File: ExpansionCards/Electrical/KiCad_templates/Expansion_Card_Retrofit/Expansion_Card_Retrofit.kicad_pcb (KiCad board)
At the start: 2 copper layers, 24 x 27.3 mm, 30 parts, among them J1 HDMI_A, P2 USB_C_Plug, U1 MS2130, U2 GD25D05CT, U3 USBLC6-2P6, Y1 Crystal

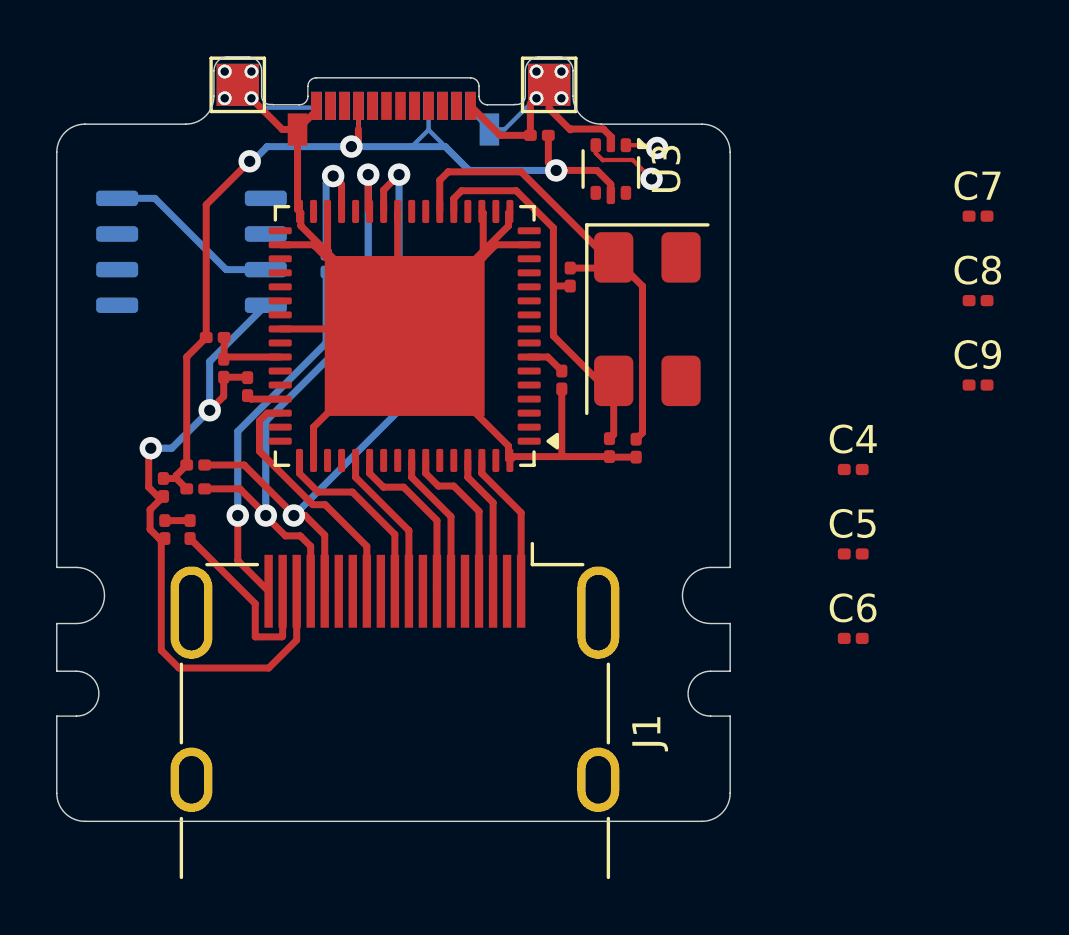
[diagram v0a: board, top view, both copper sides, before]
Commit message: Change PCB to 4 Layer and improve routing
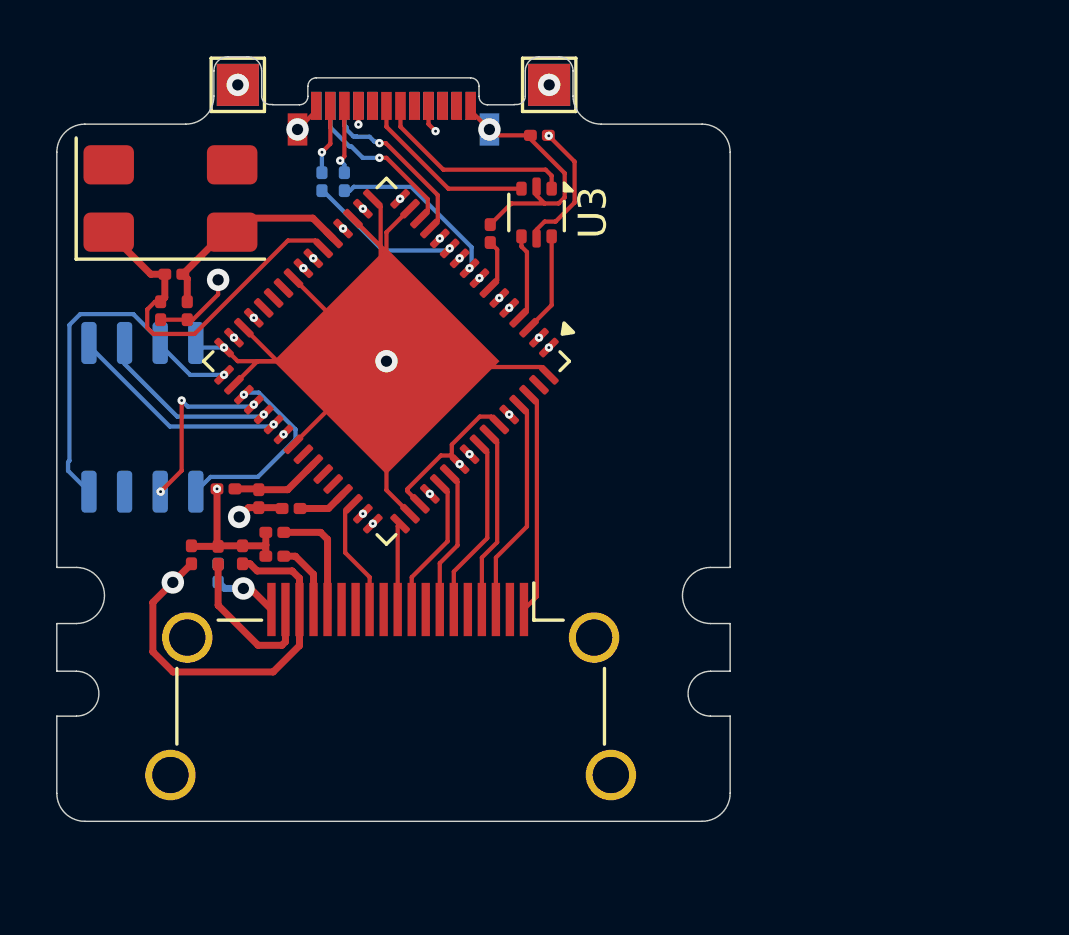
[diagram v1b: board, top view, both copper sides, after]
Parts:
- removed C4, C5, C6, C7: C_Small, Capacitor_SMD:C_0201_0603Metric
- C8, C9: moved to B.Cu
- J1: footprint Connector_Video:HDMI_A_Molex_208658-1001_Horizontal -> Connector_Video:HDMI_A_Amphenol_10029449-x01xLF_Horizontal
- moved C9 24.5 mm to (137.4, 131.8), turned to -90 degrees
- moved C8 23.0 mm to (138.2, 131.8), turned to -90 degrees
- moved C11 17.6 mm to (131.7, 136.3)
- moved Y1 17.5 mm to (132.1, 132.3), turned to 0 degrees
- moved C10 15.8 mm to (132.7, 136.3)
- moved R9 14.1 mm to (132.2, 135.1), turned to 180 degrees
- moved R3 11.7 mm to (133.8, 145.7)
- moved U2 6.15 mm to (131.1, 140.2), turned to -90 degrees
- moved R1 5.81 mm to (143.4, 133.6), turned to 90 degrees
- moved R7 5.41 mm to (134.0, 142.7)
- moved R8 4.82 mm to (135.2, 143.1)
- moved R2 4.61 mm to (136.3, 143.4), turned to 180 degrees
- moved R5 3.70 mm to (135.8, 144.2)
- moved R6 3.70 mm to (135.8, 145.1)
- moved C3 3.70 mm to (134.6, 145.1)
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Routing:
- net Net-(U2-VCC): track 6.35 -> 31.9 mm, vias 0 -> 4
- net GND: track 109.2 -> 85.4 mm, vias 10 -> 9
- net Net-(J1-SDA): track 21.3 -> 2.58 mm, vias 2 -> 0
- net Net-(J1-SCL): track 22.6 -> 4.16 mm, vias 2 -> 0
- net Net-(U1-AVDD11-Pad24): track 0.00 -> 15.5 mm, vias 0 -> 2
- net Net-(U1-AVDD25-Pad20): track 0.00 -> 12.4 mm, vias 0 -> 3
- net Net-(J1-HPD): track 13.1 -> 2.31 mm
- net Net-(U1-DVDD11-Pad18): track 0.00 -> 10.2 mm, vias 0 -> 2
- net SPICS: track 0.00 -> 7.90 mm, vias 0 -> 1
- net SPIMOSI: track 0.00 -> 7.10 mm, vias 0 -> 1
- net Net-(U1-AVDD33-Pad48): track 0.00 -> 6.89 mm, vias 0 -> 4
- net Net-(U1-XTIN): track 14.1 -> 7.53 mm
- net SPIMISO: track 0.00 -> 6.52 mm, vias 0 -> 1
- net Net-(P2-RX1-): track 0.00 -> 6.39 mm, vias 0 -> 1
- net Net-(U1-SSTXM): track 0.00 -> 6.26 mm, vias 0 -> 1
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- added copper zone on In1.Cu, net GND
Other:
- copper layers 2 -> 4
